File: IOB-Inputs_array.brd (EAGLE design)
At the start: 104.1 x 106.7 mm, 81 parts

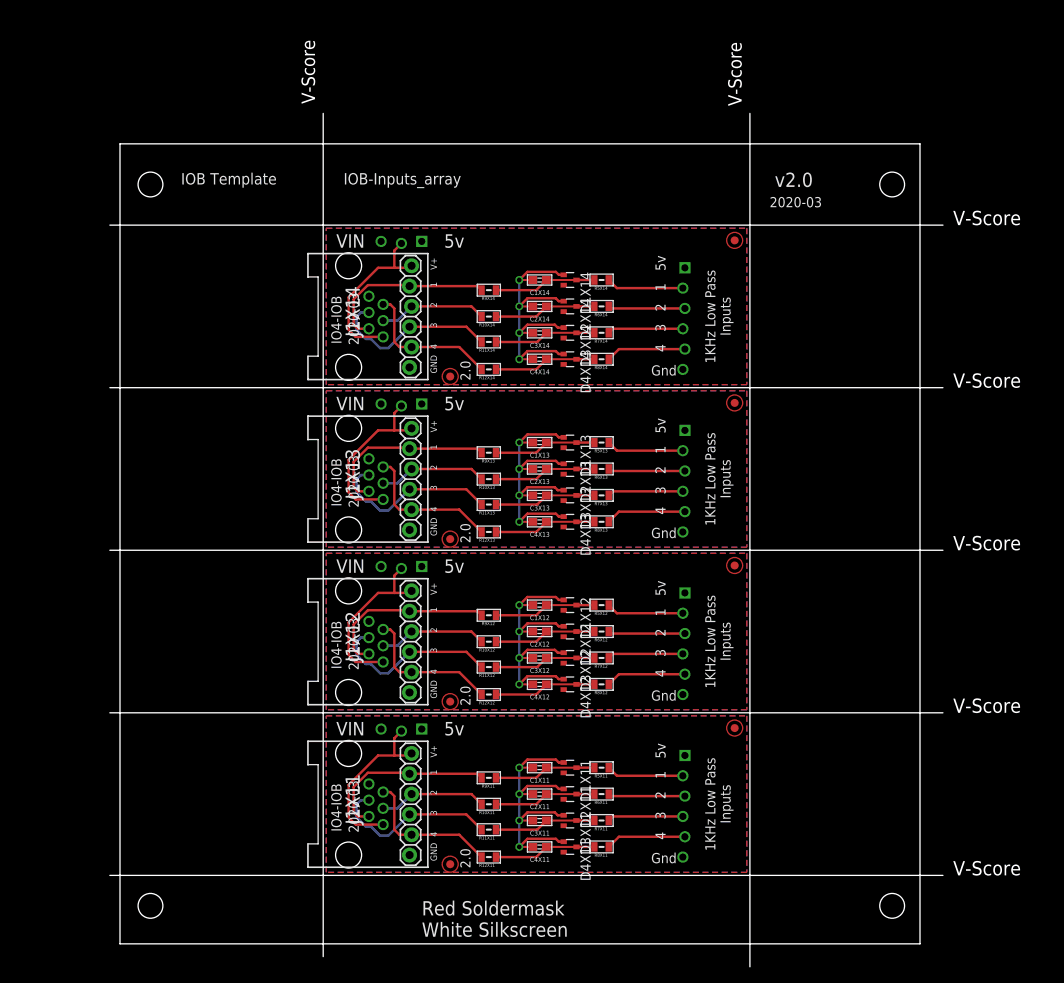
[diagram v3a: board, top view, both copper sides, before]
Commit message: built panelized array
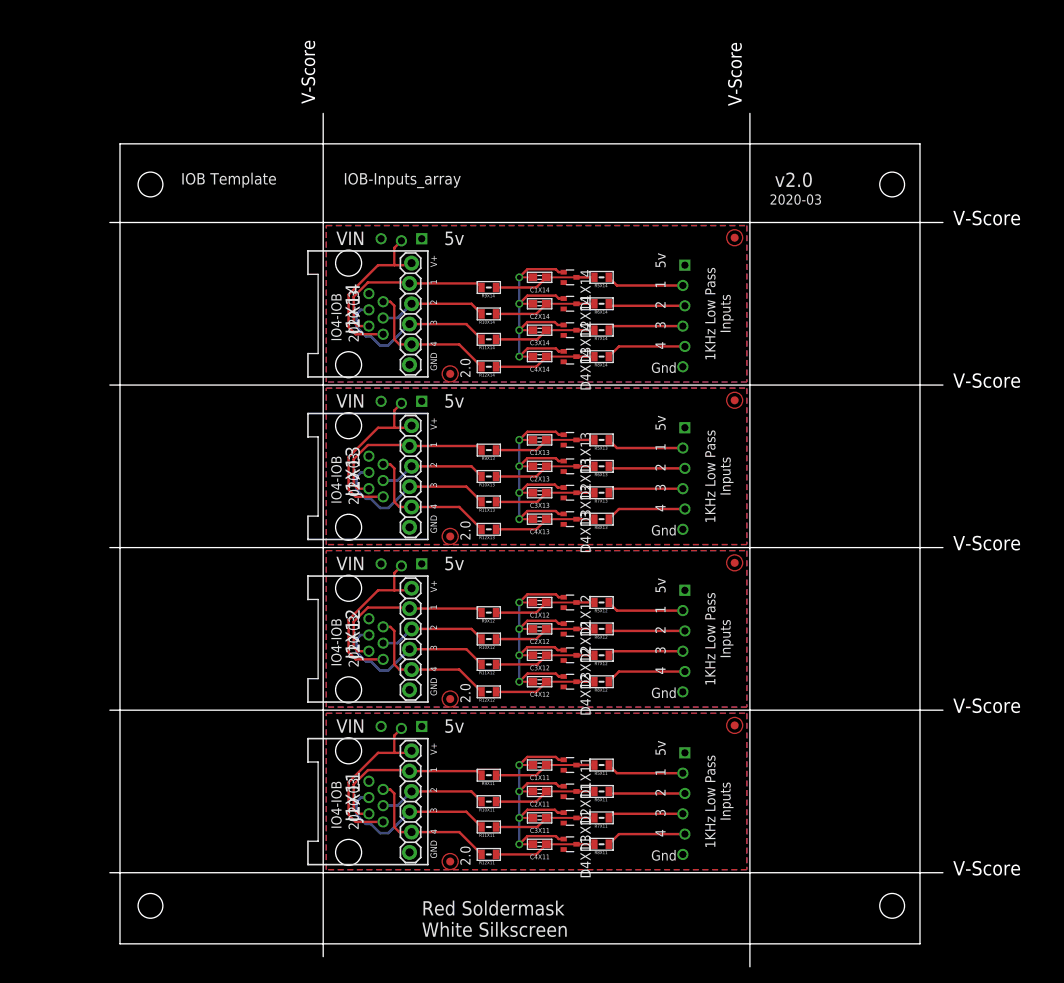
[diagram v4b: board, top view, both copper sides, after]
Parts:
- moved C2X14 0.33 mm to (52.5, 80.0)
- moved C3X14 0.33 mm to (52.5, 76.7)
- moved C4X14 0.33 mm to (52.5, 73.4)
- moved D2X14 0.33 mm to (56.3, 80.0)
- moved D3X14 0.33 mm to (56.3, 76.7)
- moved D4X14 0.33 mm to (56.3, 73.4)
- moved FID1X14 0.33 mm to (41.3, 71.2)
- moved FID2X14 0.33 mm to (76.8, 88.3)
- moved J1X12 0.33 mm to (32.4, 38.1)
- moved J1X13 0.33 mm to (32.4, 58.4)
- moved R10X12 0.33 mm to (46.1, 38.1)
- moved R10X13 0.33 mm to (46.1, 58.4)
- moved R12X13 0.33 mm to (46.1, 51.8)
- moved R6X14 0.33 mm to (60.2, 80.0)
- moved R7X14 0.33 mm to (60.2, 76.7)
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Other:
- outline, holes or cut-outs redrawn
